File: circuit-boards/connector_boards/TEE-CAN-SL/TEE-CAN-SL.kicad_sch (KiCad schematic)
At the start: 6 parts, among them J1 0705410036, J2 0705410036, J3 0705410036, J4 0705410036

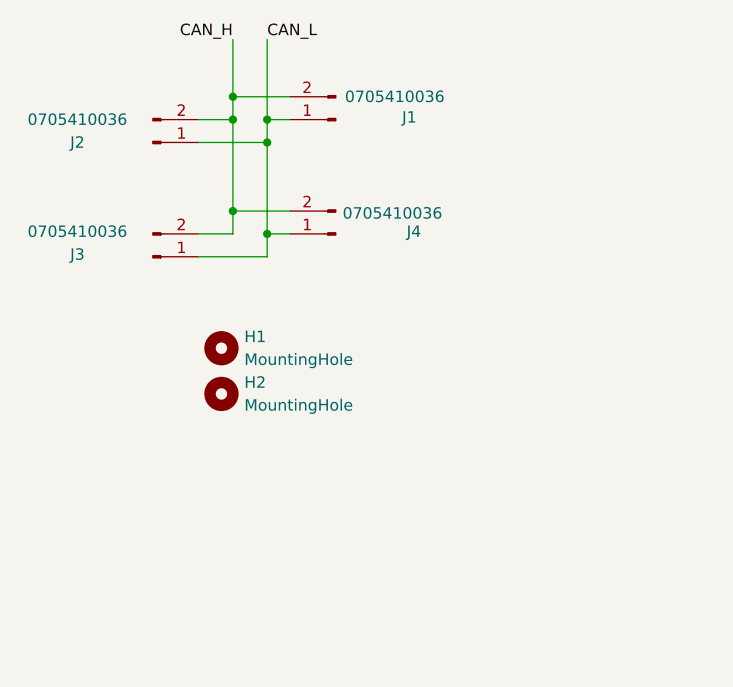
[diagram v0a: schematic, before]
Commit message: Fix pcb fab layers
Signed-off-by: Alex lenkov <Alexander.i.lenkov@gmail.com>
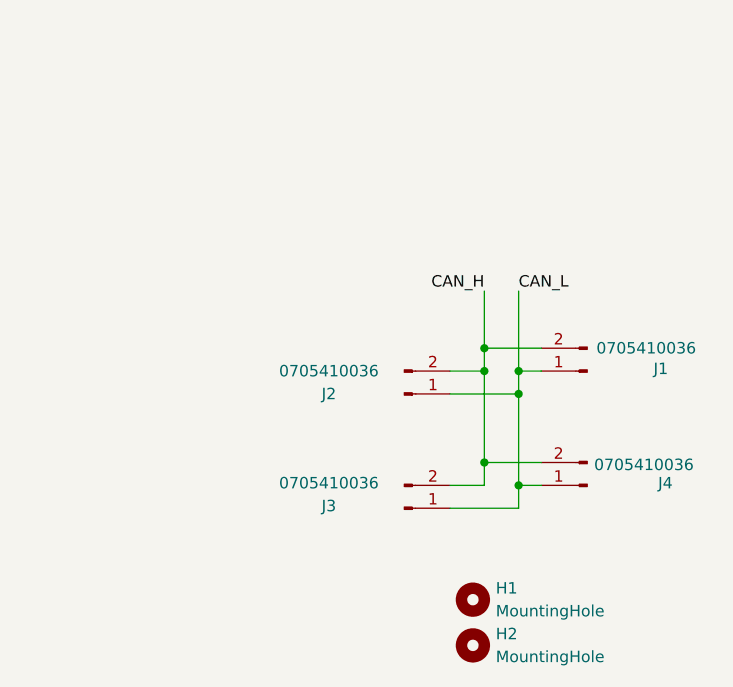
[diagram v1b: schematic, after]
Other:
- company: Spartan Robotics -> 971 SPARTAN ROBOTICS
- title: Wiedmuller -> TEE CAN SL
- moved on the sheet: H1, H2, J1, J2, J3, J4
